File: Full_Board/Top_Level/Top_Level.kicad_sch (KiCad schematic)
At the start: 3 parts

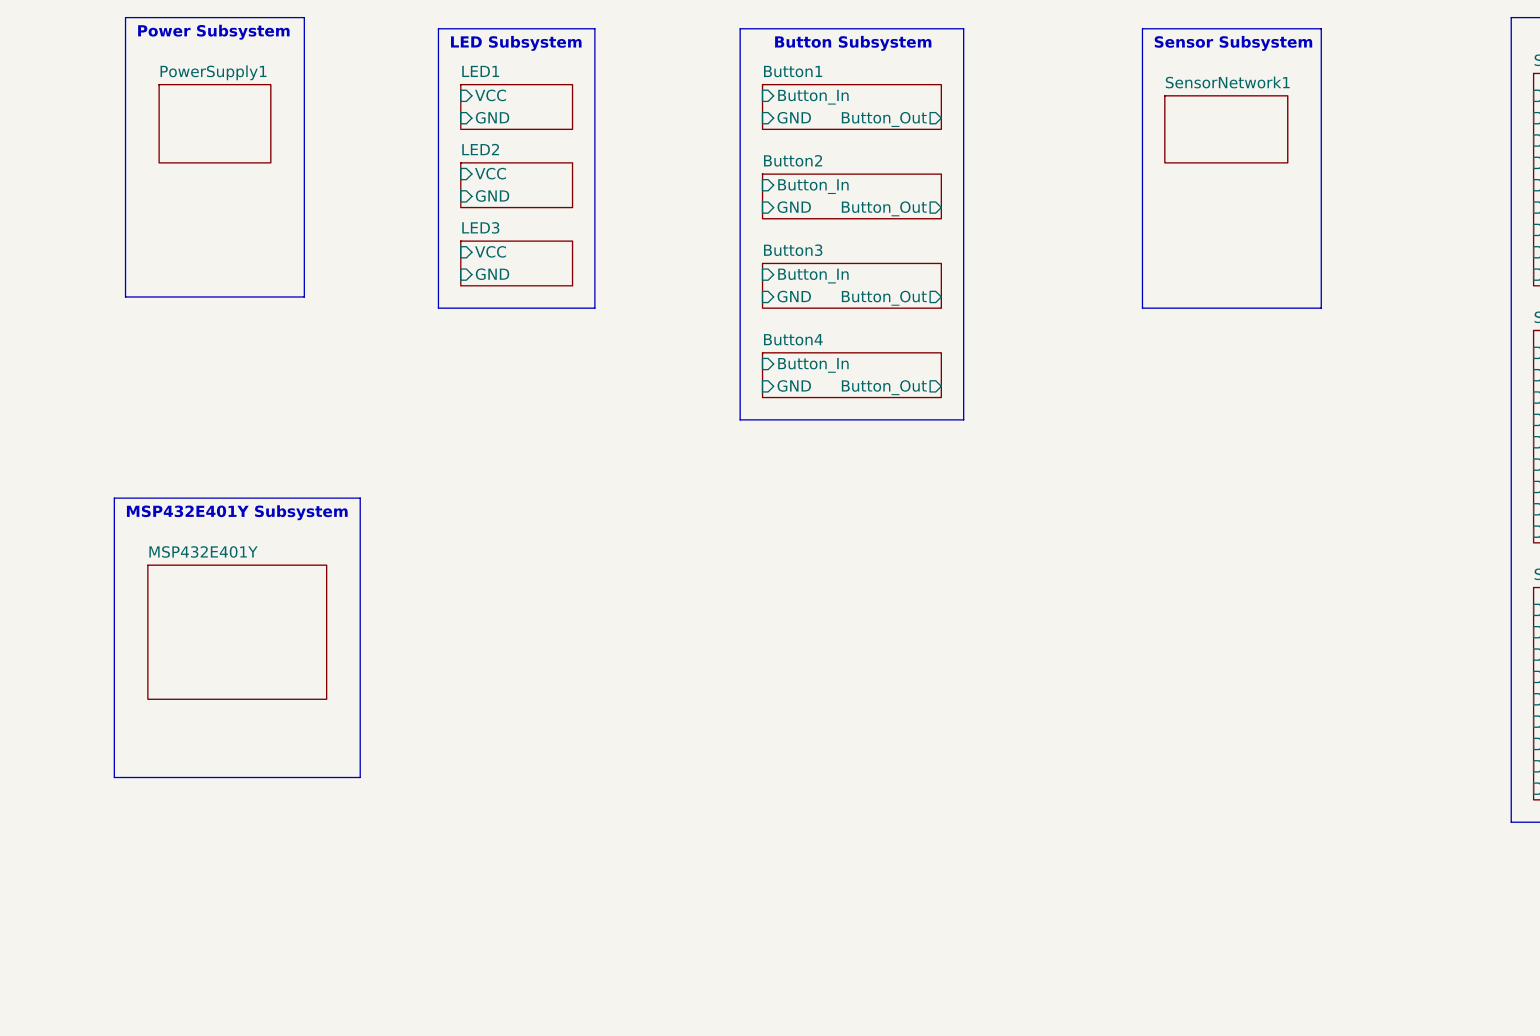
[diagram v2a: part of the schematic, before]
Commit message: Worked on Power supply subsheet
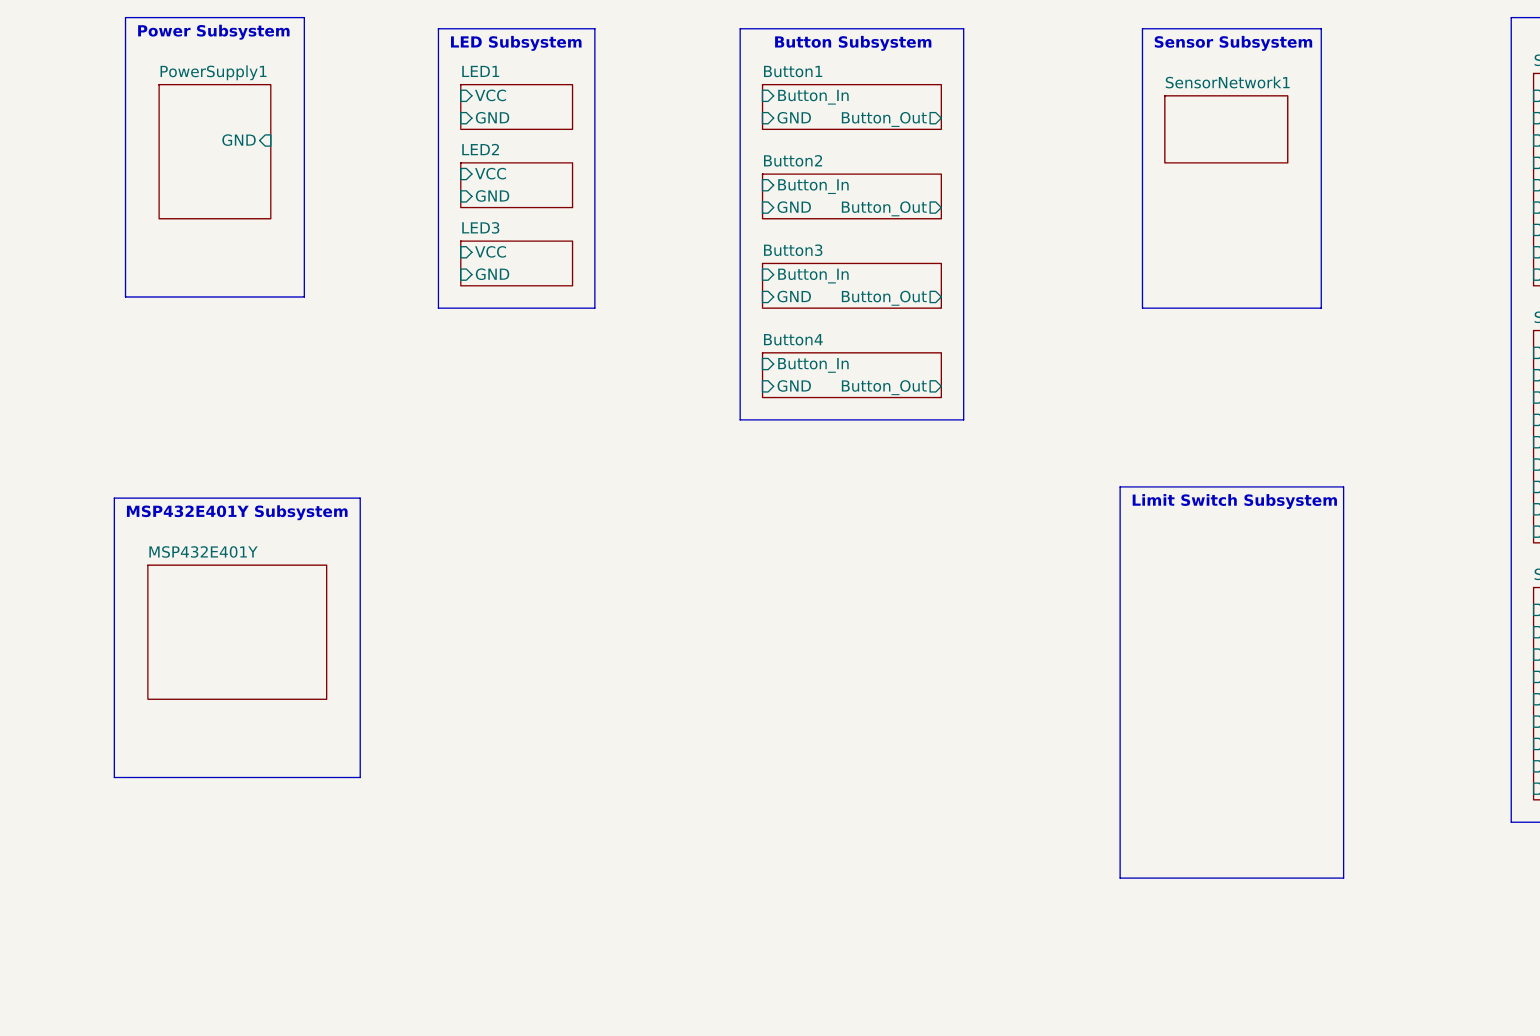
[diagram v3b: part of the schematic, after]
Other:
- sheet PowerSupply1 ports: added GND; removed none
- note added: "Limit Switch Subsystem"
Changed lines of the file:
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@@
+    (stroke (width 0) (type default) (color 0 0 0 0))
+  )
+  (polyline (pts (xy 161.29 129.54) (xy 161.29 85.09))
     (stroke (width 0) (type default) (color 0 0 0 0))
   )
@@
     (stroke (width 0) (type default) (color 0 0 0 0))
   )
+  (polyline (pts (xy 186.69 85.09) (xy 186.69 129.54))
+    (stroke (width 0) (type default) (color 0 0 0 0))
+  )
   (wire (pts (xy 105.41 171.45) (xy 105.41 172.72))
     (stroke (width 0) (type default) (color 0 0 0 0))
@@
     (stroke (width 0) (type default) (color 0 0 0 0))
   )
+  (polyline (pts (xy 161.29 85.09) (xy 186.69 85.09))
+    (stroke (width 0) (type default) (color 0 0 0 0))
+  )
   (polyline (pts (xy 118.11 33.02) (xy 143.51 33.02))
     (stroke (width 0) (type default) (color 0 0 0 0))
@@
     (stroke (width 0) (type default) (color 0 0 0 0))
   )
+  (polyline (pts (xy 186.69 129.54) (xy 161.29 129.54))
+    (stroke (width 0) (type default) (color 0 0 0 0))
+  )
   (wire (pts (xy 78.74 160.02) (xy 78.74 165.1))
     (stroke (width 0) (type default) (color 0 0 0 0))
@@
   (polyline (pts (xy 143.51 33.02) (xy 143.51 77.47))
     (stroke (width 0) (type default) (color 0 0 0 0))
+  )
+  (text "Limit Switch Subsystem" (at 162.56 87.63 0)
+    (effects (font (size 1.27 1.27) (thickness 0.254) bold) (justify left bottom))
   )
   (text "Stepper Subsystem" (at 210.82 34.29 0)
@@
     )
   )
-  (sheet (at 52.07 39.37) (size 12.7 8.89) (fields_autoplaced)
+  (sheet (at 52.07 39.37) (size 12.7 15.24) (fields_autoplaced)
     (stroke (width 0.1524) (type solid) (color 0 0 0 0))
     (fill (color 0 0 0 0.0000))
@@
       (effects (font (size 1.27 1.27)) (justify left bottom))
     )
-    (property "Sheet file" "../Power_Subsystem/PowerSupply.kicad_sch" (id 1) (at 52.07 48.8446 0)
-      (effects (font (size 1.27 1.27)) (justify left top) hide)
+    (property "Sheet file" "../Power_Subsystem/PowerSupply.kicad_sch" (id 1) (at 52.07 55.1946 0)
+      (effects (font (size 1.27 1.27)) (justify left top) hide)
+    )
+    (pin "GND" input (at 64.77 45.72 0)
+      (effects (font (size 1.27 1.27)) (justify right))
     )
   )
@@
     (path "/369b5ae9-4af3-455b-8453-a585234168a6" (page "11"))
     (path "/eed9ac13-0553-4be8-a87c-cf15a0799b3e" (page "12"))
+    (path "/e841011a-0d76-447f-b141-73da960fe0e4" (page "13"))
     (path "/85301cef-e065-48de-8b1a-931cd1e8745e" (page "13"))
-    (path "/e841011a-0d76-447f-b141-73da960fe0e4" (page "13"))
     (path "/d502e42a-f07d-48a4-870f-6cc62b560384" (page "14"))
     (path "/b2aa64e3-6d16-4ba0-adea-08cdcba55275" (page "14"))
@@
       (reference "C?") (unit 1) (value "0.01uF") (footprint "")
     )
+    (path "/85301cef-e065-48de-8b1a-931cd1e8745e/459969d4-1595-49b8-b98c-4044ef781618"
+      (reference "C?") (unit 1) (value "C") (footprint "")
+    )
+    (path "/86702842-173a-4383-816d-31c4597e63ce/466a4c0c-d5bf-4c34-98ab-cdc945d8d8b7"
+      (reference "C?") (unit 1) (value "~") (footprint "")
+    )
     (path "/0ff37166-a71a-47a9-937d-23fd840229ab/466a4c0c-d5bf-4c34-98ab-cdc945d8d8b7"
       (reference "C?") (unit 1) (value "~") (footprint "")
@@
       (reference "C?") (unit 1) (value "~") (footprint "")
     )
-    (path "/86702842-173a-4383-816d-31c4597e63ce/466a4c0c-d5bf-4c34-98ab-cdc945d8d8b7"
-      (reference "C?") (unit 1) (value "~") (footprint "")
-    )
     (path "/69c9bf85-c31a-4094-90b8-a1614b909ff9/60811976-7279-4b25-8274-54a38fc3e217"
       (reference "C?") (unit 1) (value "0.1uF") (footprint "")
@@
       (reference "C?") (unit 1) (value "0.1uF") (footprint "")
     )
+    (path "/85301cef-e065-48de-8b1a-931cd1e8745e/62bef1cb-2d31-4c3a-b6c5-6e460d83de8e"
+      (reference "C?") (unit 1) (value "C") (footprint "")
+    )
+    (path "/85301cef-e065-48de-8b1a-931cd1e8745e/67475cbf-cfc7-4607-a4fd-fac5c001c107"
+      (reference "C?") (unit 1) (value "C") (footprint "")
+    )
+    (path "/85301cef-e065-48de-8b1a-931cd1e8745e/a077b17b-0f58-4d5c-92ea-1159564768e8"
+      (reference "C?") (unit 1) (value "C") (footprint "")
+    )
     (path "/69c9bf85-c31a-4094-90b8-a1614b909ff9/b1705c0a-2d83-47c9-974e-aa5d054aa058"
       (reference "C?") (unit 1) (value "0.01uF") (footprint "")
@@
       (reference "C?") (unit 1) (value "C") (footprint "")
     )
+    (path "/85301cef-e065-48de-8b1a-931cd1e8745e/edcf626e-2640-4b11-9de4-62003070fce6"
+      (reference "C?") (unit 1) (value "C") (footprint "")
+    )
     (path "/d502e42a-f07d-48a4-870f-6cc62b560384/a80de44a-939a-45a7-aa04-16eb8d952e2b"
       (reference "D1") (unit 1) (value "~") (footprint "")
     )
+    (path "/85301cef-e065-48de-8b1a-931cd1e8745e/3d3f2e47-1bcf-4f37-b28e-126ab5b25a26"
+      (reference "D?") (unit 1) (value "D_Zener") (footprint "")
+    )
     (path "/fcb57cde-f0db-40ec-9e21-05d9382b9bd6/a80de44a-939a-45a7-aa04-16eb8d952e2b"
       (reference "D?") (unit 1) (value "~") (footprint "")
@@
       (reference "IC?") (unit 1) (value "DRV8824QPWPRQ1") (footprint "SOP65P640X120-28N")
     )
+    (path "/85301cef-e065-48de-8b1a-931cd1e8745e/226fd98f-4580-4d25-bdf9-113de3aa2d45"
+      (reference "J1") (unit 1) (value "KLDHCX-8-0202-A") (footprint "KLDHCX80202A")
+    )
     (path "/eed9ac13-0553-4be8-a87c-cf15a0799b3e/e6ba01e7-fe50-4df3-8c33-307516bbd642"
       (reference "J1-J2") (unit 1) (value "Conn_01x10") (footprint "Connector_PinSocket_2.54mm:PinSocket_2x10_P2.54mm_Vertical")
@@
       (reference "J7-J8") (unit 1) (value "Conn_01x10") (footprint "Connector_PinSocket_2.54mm:PinSocket_2x10_P2.54mm_Vertical")
     )
+    (path "/85301cef-e065-48de-8b1a-931cd1e8745e/f59ae2ed-4e5c-4dfa-b68f-07e2b93a16c2"
+      (reference "L?") (unit 1) (value "L") (footprint "")
+    )
     (path "/d502e42a-f07d-48a4-870f-6cc62b560384/46d4057d-eca7-4ce0-91a8-eed9888c23a0"
       (reference "R1") (unit 1) (value "~") (footprint "")
@@
       (reference "R3") (unit 1) (value "150") (footprint "")
     )
+    (path "/85301cef-e065-48de-8b1a-931cd1e8745e/04690b90-a286-4da0-9b1b-15dc12a1f10d"
+      (reference "R?") (unit 1) (value "R") (footprint "")
+    )
+    (path "/647404c9-5ba1-4291-8ffe-ad0ab4836cd8/46d4057d-eca7-4ce0-91a8-eed9888c23a0"
+      (reference "R?") (unit 1) (value "~") (footprint "")
+    )
     (path "/fcb57cde-f0db-40ec-9e21-05d9382b9bd6/46d4057d-eca7-4ce0-91a8-eed9888c23a0"
       (reference "R?") (unit 1) (value "~") (footprint "")
     )
-    (path "/647404c9-5ba1-4291-8ffe-ad0ab4836cd8/46d4057d-eca7-4ce0-91a8-eed9888c23a0"
+    (path "/ebc80814-4044-4d9b-87c5-771a37b035bf/63e35775-33c8-4477-b48f-0df8d0323ed6"
+      (reference "R?") (unit 1) (value "~") (footprint "")
+    )
+    (path "/86702842-173a-4383-816d-31c4597e63ce/63e35775-33c8-4477-b48f-0df8d0323ed6"
       (reference "R?") (unit 1) (value "~") (footprint "")
     )
@@
       (reference "R?") (unit 1) (value "~") (footprint "")
     )
-    (path "/ebc80814-4044-4d9b-87c5-771a37b035bf/63e35775-33c8-4477-b48f-0df8d0323ed6"
-      (reference "R?") (unit 1) (value "~") (footprint "")
-    )
-    (path "/86702842-173a-4383-816d-31c4597e63ce/63e35775-33c8-4477-b48f-0df8d0323ed6"
-      (reference "R?") (unit 1) (value "~") (footprint "")
+    (path "/85301cef-e065-48de-8b1a-931cd1e8745e/afbaf16a-17c6-47c8-82be-471ae180ffb4"
+      (reference "R?") (unit 1) (value "R") (footprint "")
     )
     (path "/69c9bf85-c31a-4094-90b8-a1614b909ff9/c176aa07-083e-46f1-bf2c-c3174fc9d66a"
@@
       (reference "R?") (unit 1) (value "150") (footprint "")
     )
+    (path "/69c9bf85-c31a-4094-90b8-a1614b909ff9/f2bad6f9-5260-4af4-9379-539907a77a3f"
+      (reference "R?") (unit 1) (value "150") (footprint "")
+    )
     (path "/84630889-4c81-4427-b227-6a7d31e9afff/f2bad6f9-5260-4af4-9379-539907a77a3f"
       (reference "R?") (unit 1) (value "150") (footprint "")
     )
-    (path "/69c9bf85-c31a-4094-90b8-a1614b909ff9/f2bad6f9-5260-4af4-9379-539907a77a3f"
-      (reference "R?") (unit 1) (value "150") (footprint "")
-    )
     (path "/e841011a-0d76-447f-b141-73da960fe0e4/6fb9daa2-9805-44cc-a039-5db42ed87dcc"
       (reference "SW1") (unit 1) (value "~") (footprint "")
     )
+    (path "/ebc80814-4044-4d9b-87c5-771a37b035bf/6fb9daa2-9805-44cc-a039-5db42ed87dcc"
+      (reference "SW?") (unit 1) (value "~") (footprint "")
+    )
+    (path "/86702842-173a-4383-816d-31c4597e63ce/6fb9daa2-9805-44cc-a039-5db42ed87dcc"
+      (reference "SW?") (unit 1) (value "~") (footprint "")
+    )
     (path "/0ff37166-a71a-47a9-937d-23fd840229ab/6fb9daa2-9805-44cc-a039-5db42ed87dcc"
       (reference "SW?") (unit 1) (value "~") (footprint "")
     )
-    (path "/ebc80814-4044-4d9b-87c5-771a37b035bf/6fb9daa2-9805-44cc-a039-5db42ed87dcc"
-      (reference "SW?") (unit 1) (value "~") (footprint "")
-    )
-    (path "/86702842-173a-4383-816d-31c4597e63ce/6fb9daa2-9805-44cc-a039-5db42ed87dcc"
-      (reference "SW?") (unit 1) (value "~") (footprint "")
-    )
-  )
+    (path "/85301cef-e065-48de-8b1a-931cd1e8745e/d748fcc1-f39f-45dd-84be-96afbe01d067"
+      (reference "TP1") (unit 1) (value "TestPoint") (footprint "TestPoint:TestPoint_Keystone_5010-5014_Multipurpose")
+    )
+    (path "/85301cef-e065-48de-8b1a-931cd1e8745e/4254629d-5025-4fa7-bce7-820d59c81b8c"
+      (reference "TP2") (unit 1) (value "TestPoint") (footprint "TestPoint:TestPoint_Keystone_5010-5014_Multipurpose")
+    )
+    (path "/85301cef-e065-48de-8b1a-931cd1e8745e/22b034aa-6a45-4150-9a06-bda960605f66"
+      (reference "TP3") (unit 1) (value "TestPoint") (footprint "TestPoint:TestPoint_Keystone_5010-5014_Multipurpose")
+    )
+    (path "/85301cef-e065-48de-8b1a-931cd1e8745e/785124af-9db7-4e4c-8e56-3baebf054462"
+      (reference "TP4") (unit 1) (value "TestPoint") (footprint "TestPoint:TestPoint_Keystone_5010-5014_Multipurpose")
+    )
+    (path "/85301cef-e065-48de-8b1a-931cd1e8745e/1166b0ea-f99b-4604-9f82-ca8cd3e7e945"
+      (reference "U?") (unit 1) (value "TPS5403DR") (footprint "D0008A_N")
+    )
+  )
